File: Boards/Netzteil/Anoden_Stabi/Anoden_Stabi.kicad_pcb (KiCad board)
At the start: 2 copper layers, 100 x 80 mm, 25 parts, among them J1 Conn_01x06, P1 CONN_3, Q1 2SC2979, Q2 MJE5731

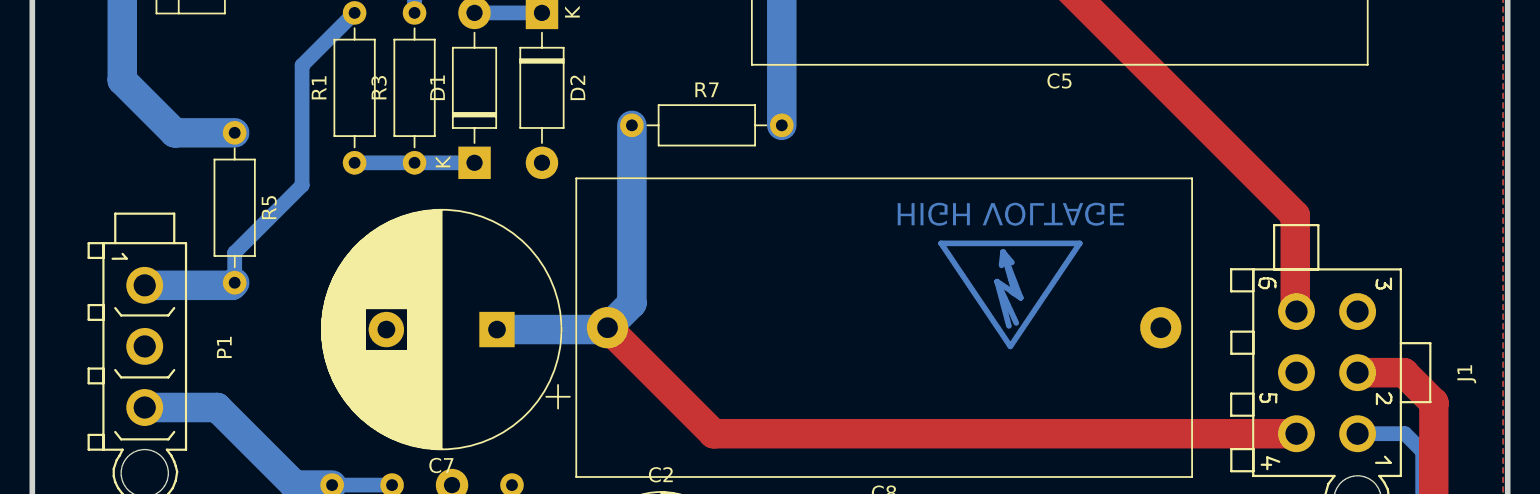
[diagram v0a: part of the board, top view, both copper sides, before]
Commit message: Added Test, moved mounting holes
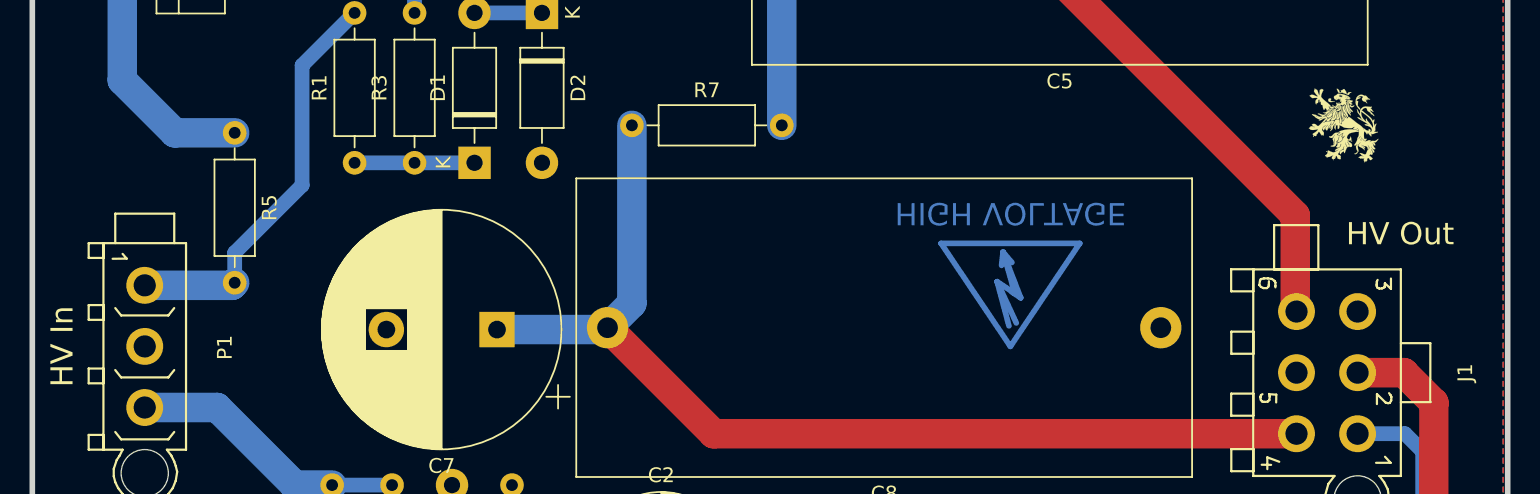
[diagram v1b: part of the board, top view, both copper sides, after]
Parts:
- added G***: LOGO, Loewe:Loewe_Klein, F.Cu at (165.1, 75.2)
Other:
- board text added: "HV In"
- board text added: "HV Out"

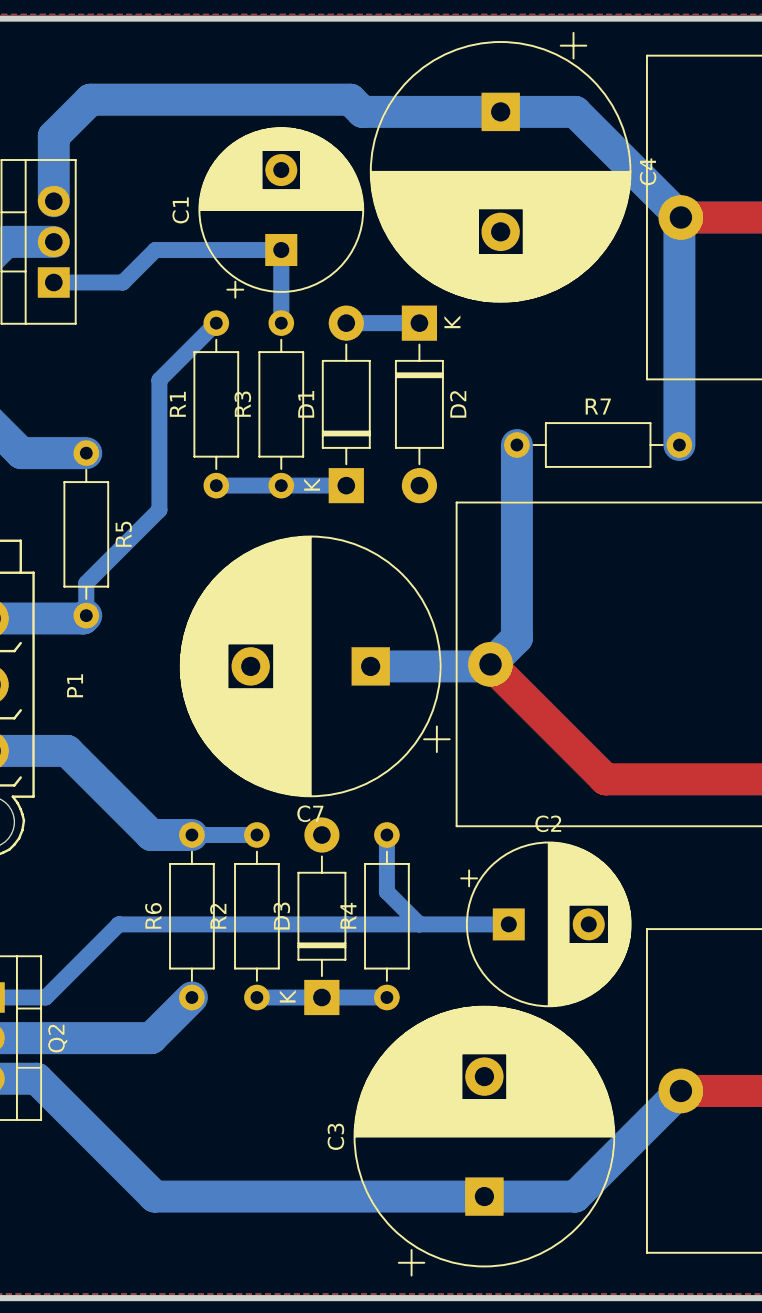
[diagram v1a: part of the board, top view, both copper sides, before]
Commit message: Adjusted Silkscreen
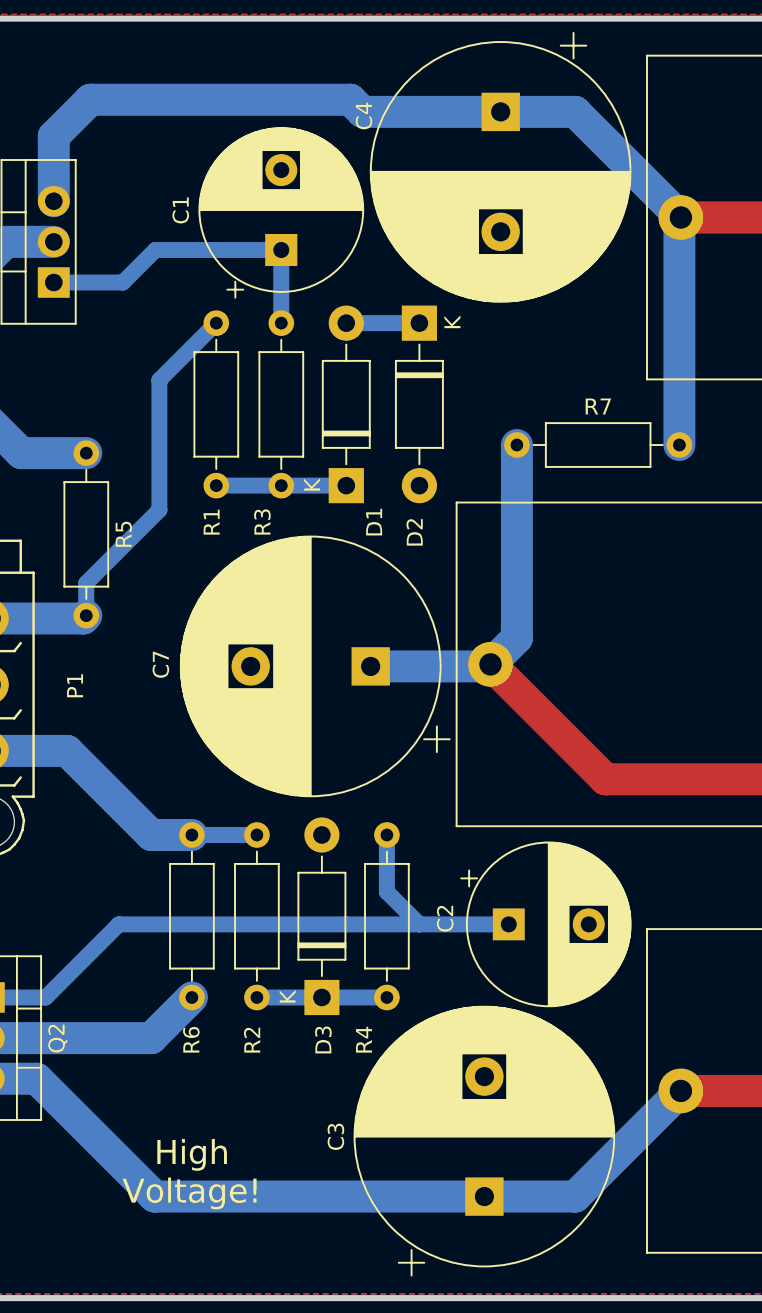
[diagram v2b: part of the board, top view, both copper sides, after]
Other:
- board text added: "High Voltage!"
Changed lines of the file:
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@@
   (general
     (thickness 1.6)
-    (drawings 4)
+    (drawings 5)
     (tracks 76)
     (zones 0)
@@
     (descr "Resistor, Axial_DIN0207 series, Axial, Horizontal, pin pitch=10.16mm, 0.25W = 1/4W, length*diameter=6.3*2.5mm^2, http://cdn-reichelt.de/documents/datenblatt/B400/1_4W%23YAG.pdf")
     (tags "Resistor Axial_DIN0207 series Axial Horizontal pin pitch 10.16mm 0.25W = 1/4W length 6.3mm diameter 2.5mm")
-    (fp_text reference R6 (at 5.08 -2.37 90) (layer F.SilkS)
+    (fp_text reference R6 (at -2.667 0 90) (layer F.SilkS)
       (effects (font (size 1 1) (thickness 0.15)))
     )
@@
     (descr "Resistor, Axial_DIN0207 series, Axial, Horizontal, pin pitch=10.16mm, 0.25W = 1/4W, length*diameter=6.3*2.5mm^2, http://cdn-reichelt.de/documents/datenblatt/B400/1_4W%23YAG.pdf")
     (tags "Resistor Axial_DIN0207 series Axial Horizontal pin pitch 10.16mm 0.25W = 1/4W length 6.3mm diameter 2.5mm")
-    (fp_text reference R4 (at 5.08 -2.37 90) (layer F.SilkS)
+    (fp_text reference R4 (at -2.667 -1.397 90) (layer F.SilkS)
       (effects (font (size 1 1) (thickness 0.15)))
     )
@@
     (descr "Resistor, Axial_DIN0207 series, Axial, Horizontal, pin pitch=10.16mm, 0.25W = 1/4W, length*diameter=6.3*2.5mm^2, http://cdn-reichelt.de/documents/datenblatt/B400/1_4W%23YAG.pdf")
     (tags "Resistor Axial_DIN0207 series Axial Horizontal pin pitch 10.16mm 0.25W = 1/4W length 6.3mm diameter 2.5mm")
-    (fp_text reference R3 (at 5.08 -2.37 90) (layer F.SilkS)
+    (fp_text reference R3 (at -2.286 -1.143 90) (layer F.SilkS)
       (effects (font (size 1 1) (thickness 0.15)))
     )
@@
     (descr "Resistor, Axial_DIN0207 series, Axial, Horizontal, pin pitch=10.16mm, 0.25W = 1/4W, length*diameter=6.3*2.5mm^2, http://cdn-reichelt.de/documents/datenblatt/B400/1_4W%23YAG.pdf")
     (tags "Resistor Axial_DIN0207 series Axial Horizontal pin pitch 10.16mm 0.25W = 1/4W length 6.3mm diameter 2.5mm")
-    (fp_text reference R2 (at 5.08 -2.37 90) (layer F.SilkS)
+    (fp_text reference R2 (at -2.667 -0.254 90) (layer F.SilkS)
       (effects (font (size 1 1) (thickness 0.15)))
     )
@@
     (descr "Resistor, Axial_DIN0207 series, Axial, Horizontal, pin pitch=10.16mm, 0.25W = 1/4W, length*diameter=6.3*2.5mm^2, http://cdn-reichelt.de/documents/datenblatt/B400/1_4W%23YAG.pdf")
     (tags "Resistor Axial_DIN0207 series Axial Horizontal pin pitch 10.16mm 0.25W = 1/4W length 6.3mm diameter 2.5mm")
-    (fp_text reference R1 (at 5.08 -2.37 90) (layer F.SilkS)
+    (fp_text reference R1 (at -2.286 -0.254 90) (layer F.SilkS)
       (effects (font (size 1 1) (thickness 0.15)))
     )
@@
     (descr "Diode, DO-41_SOD81 series, Axial, Horizontal, pin pitch=10.16mm, , length*diameter=5.2*2.7mm^2, , http://www.diodes.com/_files/packages/DO-41%20(Plastic).pdf")
     (tags "Diode DO-41_SOD81 series Axial Horizontal pin pitch 10.16mm  length 5.2mm diameter 2.7mm")
-    (fp_text reference D3 (at 5.08 -2.47 90) (layer F.SilkS)
+    (fp_text reference D3 (at -2.667 0.127 90) (layer F.SilkS)
       (effects (font (size 1 1) (thickness 0.15)))
     )
@@
     (descr "Diode, DO-41_SOD81 series, Axial, Horizontal, pin pitch=10.16mm, , length*diameter=5.2*2.7mm^2, , http://www.diodes.com/_files/packages/DO-41%20(Plastic).pdf")
     (tags "Diode DO-41_SOD81 series Axial Horizontal pin pitch 10.16mm  length 5.2mm diameter 2.7mm")
-    (fp_text reference D2 (at 5.08 -2.47 270) (layer F.SilkS)
+    (fp_text reference D2 (at 13.081 0.254 270) (layer F.SilkS)
       (effects (font (size 1 1) (thickness 0.15)))
     )
@@
     (descr "Diode, DO-41_SOD81 series, Axial, Horizontal, pin pitch=10.16mm, , length*diameter=5.2*2.7mm^2, , http://www.diodes.com/_files/packages/DO-41%20(Plastic).pdf")
     (tags "Diode DO-41_SOD81 series Axial Horizontal pin pitch 10.16mm  length 5.2mm diameter 2.7mm")
-    (fp_text reference D1 (at 5.08 -2.47 90) (layer F.SilkS)
+    (fp_text reference D1 (at -2.286 1.778 90) (layer F.SilkS)
       (effects (font (size 1 1) (thickness 0.15)))
     )
@@
     (descr "CP, Radial series, Radial, pin pitch=7.50mm, , diameter=16mm, Electrolytic Capacitor")
     (tags "CP Radial series Radial pin pitch 7.50mm  diameter 16mm Electrolytic Capacitor")
-    (fp_text reference C7 (at 3.75 -9.25 180) (layer F.SilkS)
+    (fp_text reference C7 (at 13.081 0.127 270) (layer F.SilkS)
       (effects (font (size 1 1) (thickness 0.15)))
     )
@@
     (descr "CP, Radial series, Radial, pin pitch=7.50mm, , diameter=16mm, Electrolytic Capacitor")
     (tags "CP Radial series Radial pin pitch 7.50mm  diameter 16mm Electrolytic Capacitor")
-    (fp_text reference C4 (at 3.75 -9.25 270) (layer F.SilkS)
+    (fp_text reference C4 (at 0.254 8.509 270) (layer F.SilkS)
       (effects (font (size 1 1) (thickness 0.15)))
     )
@@
     (descr "CP, Radial series, Radial, pin pitch=5.00mm, , diameter=10mm, Electrolytic Capacitor")
     (tags "CP Radial series Radial pin pitch 5.00mm  diameter 10mm Electrolytic Capacitor")
-    (fp_text reference C2 (at 2.5 -6.25) (layer F.SilkS)
+    (fp_text reference C2 (at -3.937 -0.381 90) (layer F.SilkS)
       (effects (font (size 1 1) (thickness 0.15)))
     )
@@
     (pad "" np_thru_hole circle (at 8.59028 -2.0701 270) (size 3.2004 3.2004) (drill 3.2004) (layers *.Cu *.Mask))
   )
+  (gr_text "High\nVoltage!" (at 96.52 120.65) (layer F.SilkS)
+    (effects (font (size 1.5 1.5) (thickness 0.3)))
+  )
   (gr_text "HV In" (at 78.232 90.17 90) (layer F.SilkS)

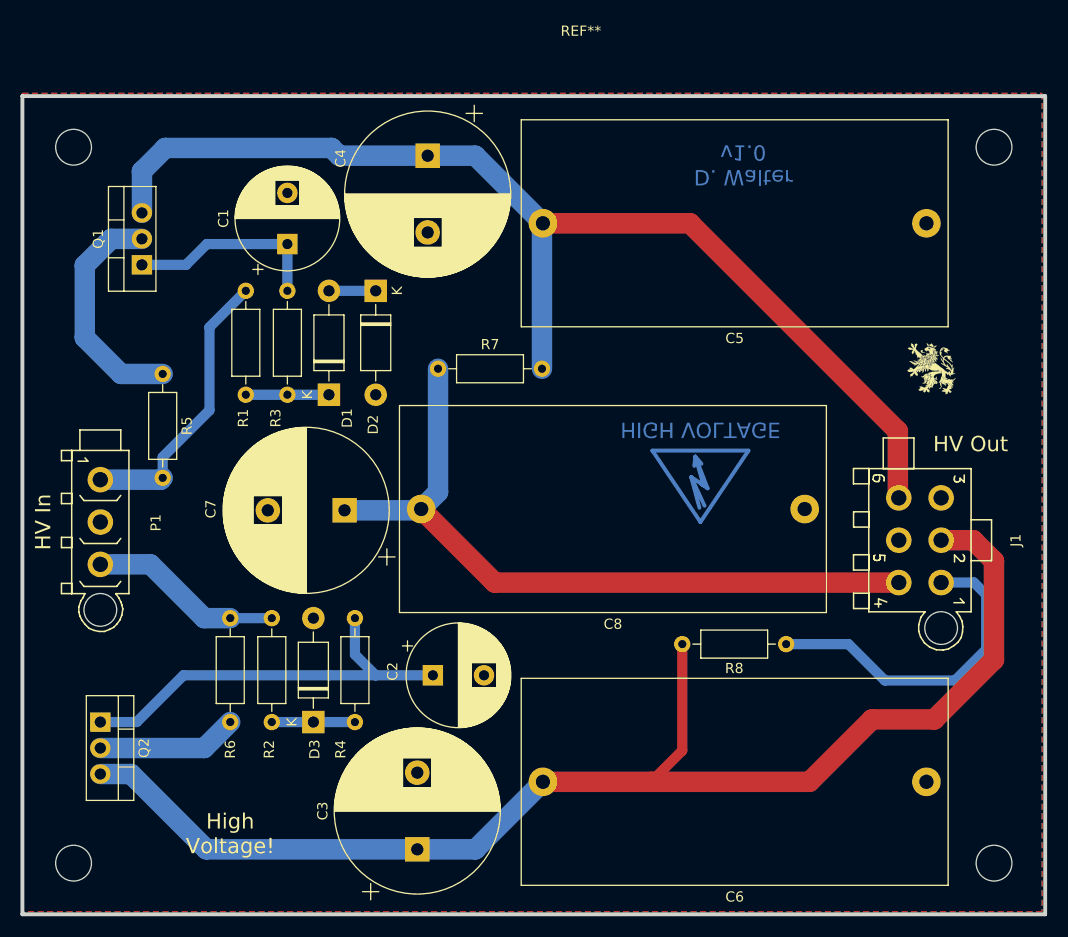
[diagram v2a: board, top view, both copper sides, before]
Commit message: Added Mounting holes, Moved -60V Divider to HV Board, eliminated +450V Connector and Feedback Connector on Amp Board
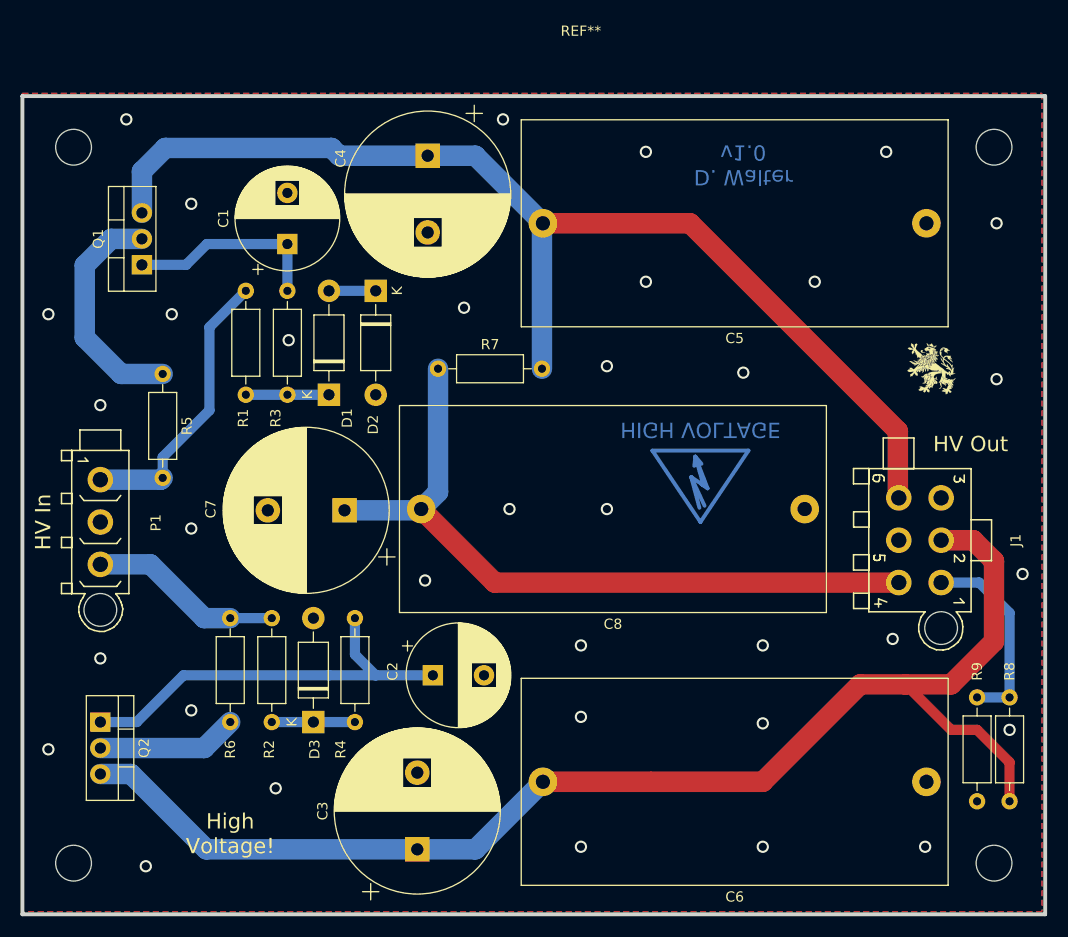
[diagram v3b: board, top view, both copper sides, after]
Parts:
- added R9: 10k, Resistor_THT:R_Axial_DIN0207_L6.3mm_D2.5mm_P10.16mm_Horizontal, F.Cu at (169.5, 117.5)
- moved R8 22.5 mm to (172.7, 107.3), turned to 270 degrees
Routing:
- net -60V: track 32.5 -> 19.4 mm
- net -120V: track 128.6 -> 129.9 mm
- net GND: vias 0 -> 35

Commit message: 6,3V und 12V auf einer Platine zusammengefasst
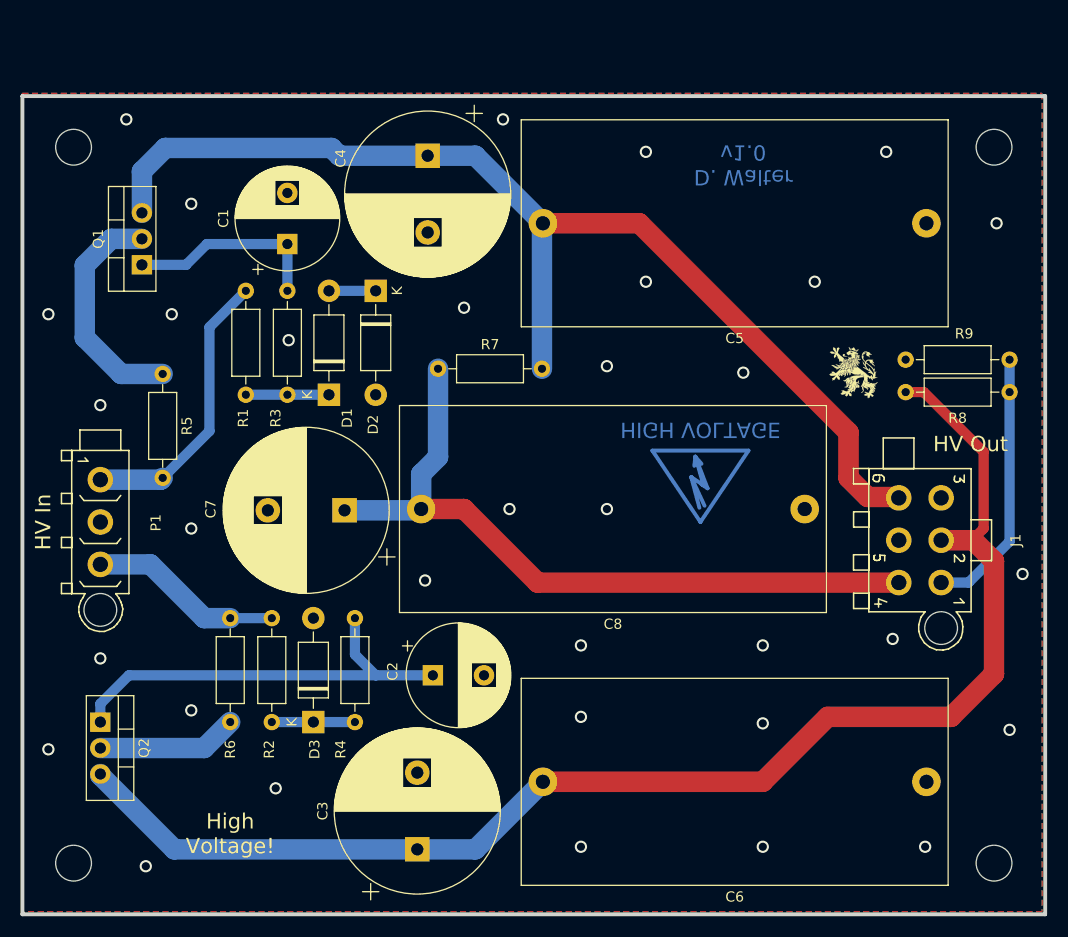
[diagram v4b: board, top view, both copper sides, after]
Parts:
- moved R9 43.7 mm to (162.6, 74.3), turned to 0 degrees
- moved R8 29.8 mm to (172.7, 77.5), turned to 180 degrees
- moved G*** 7.63 mm to (157.5, 75.6)
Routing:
- net -120V: track 129.9 -> 136.9 mm
- net -60V: track 19.4 -> 26.1 mm
- net +300V: track 111.3 -> 110.1 mm
- net Net-(C2-Pad1): track 40.8 -> 41.9 mm
- net GND: vias 35 -> 34
